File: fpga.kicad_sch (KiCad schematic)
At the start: 13 parts, among them U1 LFE5U-25F-6BG256x

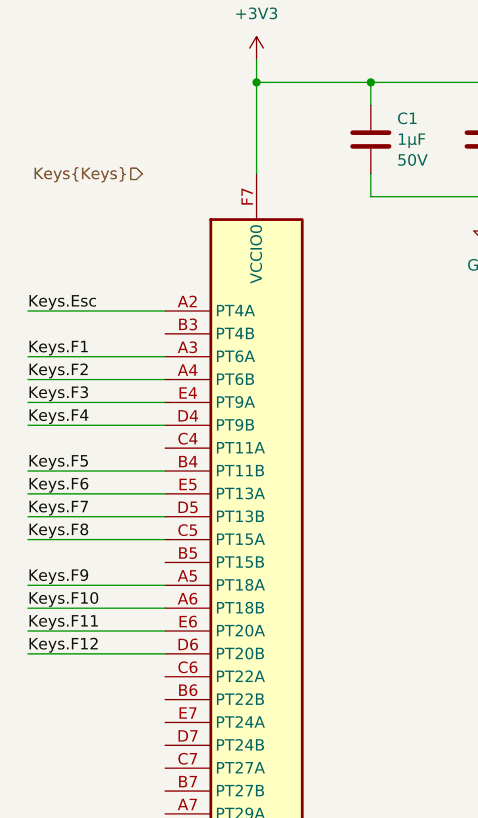
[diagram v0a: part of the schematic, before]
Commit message: Add all keys
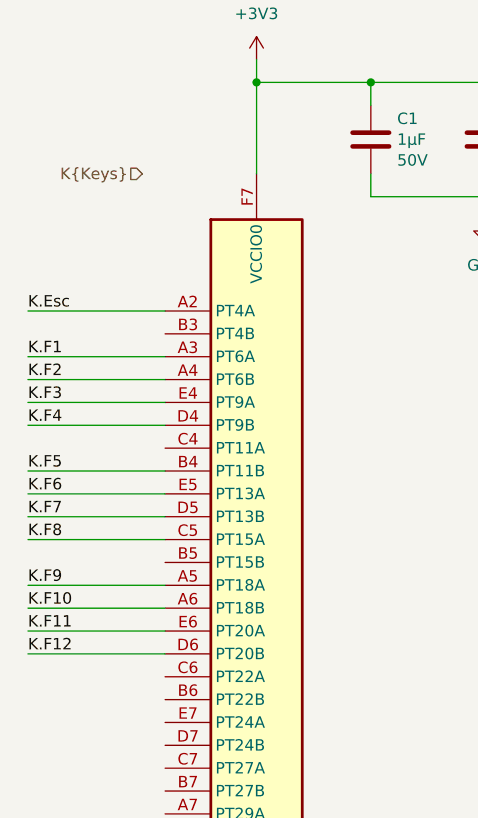
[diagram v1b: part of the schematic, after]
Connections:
- net Keys.Esc renamed K.Esc
- net Keys.F1 renamed K.F1
- net Keys.F10 renamed K.F10
- net Keys.F11 renamed K.F11
- net Keys.F12 renamed K.F12
- net Keys.F2 renamed K.F2
- net Keys.F3 renamed K.F3
- net Keys.F4 renamed K.F4
- net Keys.F5 renamed K.F5
- net Keys.F6 renamed K.F6
- net Keys.F7 renamed K.F7
- net Keys.F8 renamed K.F8
- net Keys.F9 renamed K.F9
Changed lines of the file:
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@@
 		)
 	)
-	(label "Keys.F9"
+	(label "K.F9"
 		(at 25.4 83.82 0)
 		(effects
@@
 		)
 	)
-	(label "Keys.F1"
+	(label "K.F1"
 		(at 25.4 58.42 0)
 		(effects
@@
 		)
 	)
-	(label "Keys.F4"
+	(label "K.F4"
 		(at 25.4 66.04 0)
 		(effects
@@
 		)
 	)
-	(label "Keys.F5"
+	(label "K.F5"
 		(at 25.4 71.12 0)
 		(effects
@@
 		)
 	)
-	(label "Keys.F7"
+	(label "K.F7"
 		(at 25.4 76.2 0)
 		(effects
@@
 		)
 	)
-	(label "Keys.Esc"
+	(label "K.Esc"
 		(at 25.4 53.34 0)
 		(effects
@@
 		)
 	)
-	(label "Keys.F6"
+	(label "K.F6"
 		(at 25.4 73.66 0)
 		(effects
@@
 		)
 	)
-	(label "Keys.F10"
+	(label "K.F10"
 		(at 25.4 86.36 0)
 		(effects
@@
 		)
 	)
-	(label "Keys.F12"
+	(label "K.F12"
 		(at 25.4 91.44 0)
 		(effects
@@
 		)
 	)
-	(label "Keys.F11"
+	(label "K.F11"
 		(at 25.4 88.9 0)
 		(effects
@@
 		)
 	)
-	(label "Keys.F2"
+	(label "K.F2"
 		(at 25.4 60.96 0)
 		(effects
@@
 		)
 	)
-	(label "Keys.F3"
+	(label "K.F3"
 		(at 25.4 63.5 0)
 		(effects
@@
 		)
 	)
-	(label "Keys.F8"
+	(label "K.F8"
 		(at 25.4 78.74 0)
 		(effects
@@
 		)
 	)
-	(hierarchical_label "Keys{Keys}"
+	(hierarchical_label "K{Keys}"
 		(shape input)
 		(at 38.1 38.1 180)

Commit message: Initial commit of the PCB
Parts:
- added C13: 1µF, Capacitor_SMD:C_0603_1608Metric, symbol Device:C
- added Y1: KC2520Z, Oscillator:Oscillator_SMD_Kyocera_KC2520Z-4Pin_2.5x2.0mm, symbol Oscillator:KC2520Z
- U1: footprint (none) -> Package_BGA:BGA-256_14.0x14.0mm_Layout16x16_P0.8mm_Ball0.45mm_Pad0.32mm_NSMD
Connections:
- net +3V3: now also C13.1, Y1.4 (VCC)
- net GND: now also C13.2, Y1.2 (GND)
- net CLK_48MHz: now reaches U1.M1 (PL26C)
- net CLK_48MHz: now also Y1.3 (CLK)
- no-connect marks 0 -> 1
